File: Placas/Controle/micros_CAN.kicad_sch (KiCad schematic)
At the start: 8 parts, among them J10 Conn_01x02_Pin, J11 Conn_01x02_Pin, U10 ESP32-DevKitC, U8 ESP32-DevKitC, U9 TJA1050

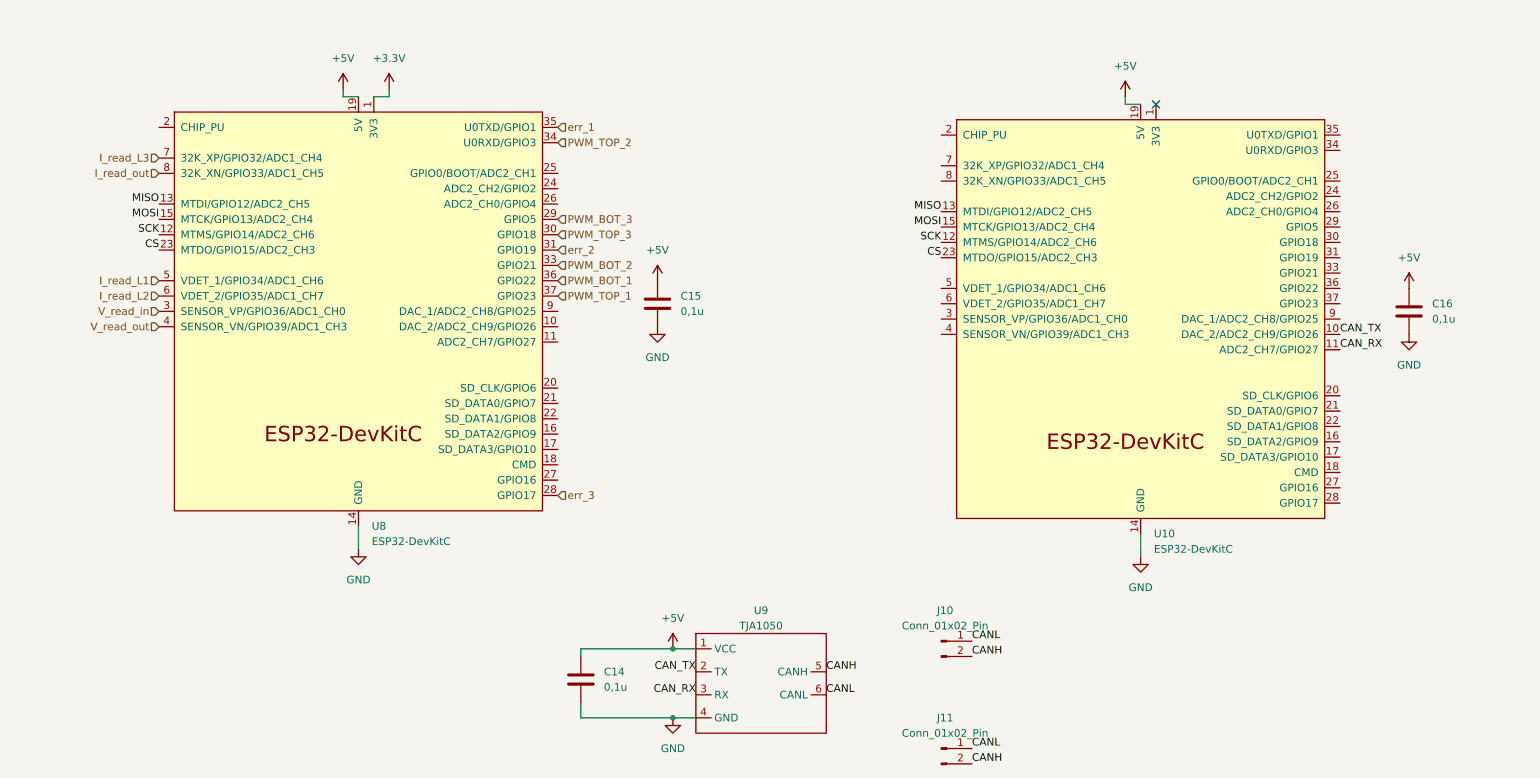
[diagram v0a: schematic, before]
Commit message: Adição de circuitos opcionais para PWM
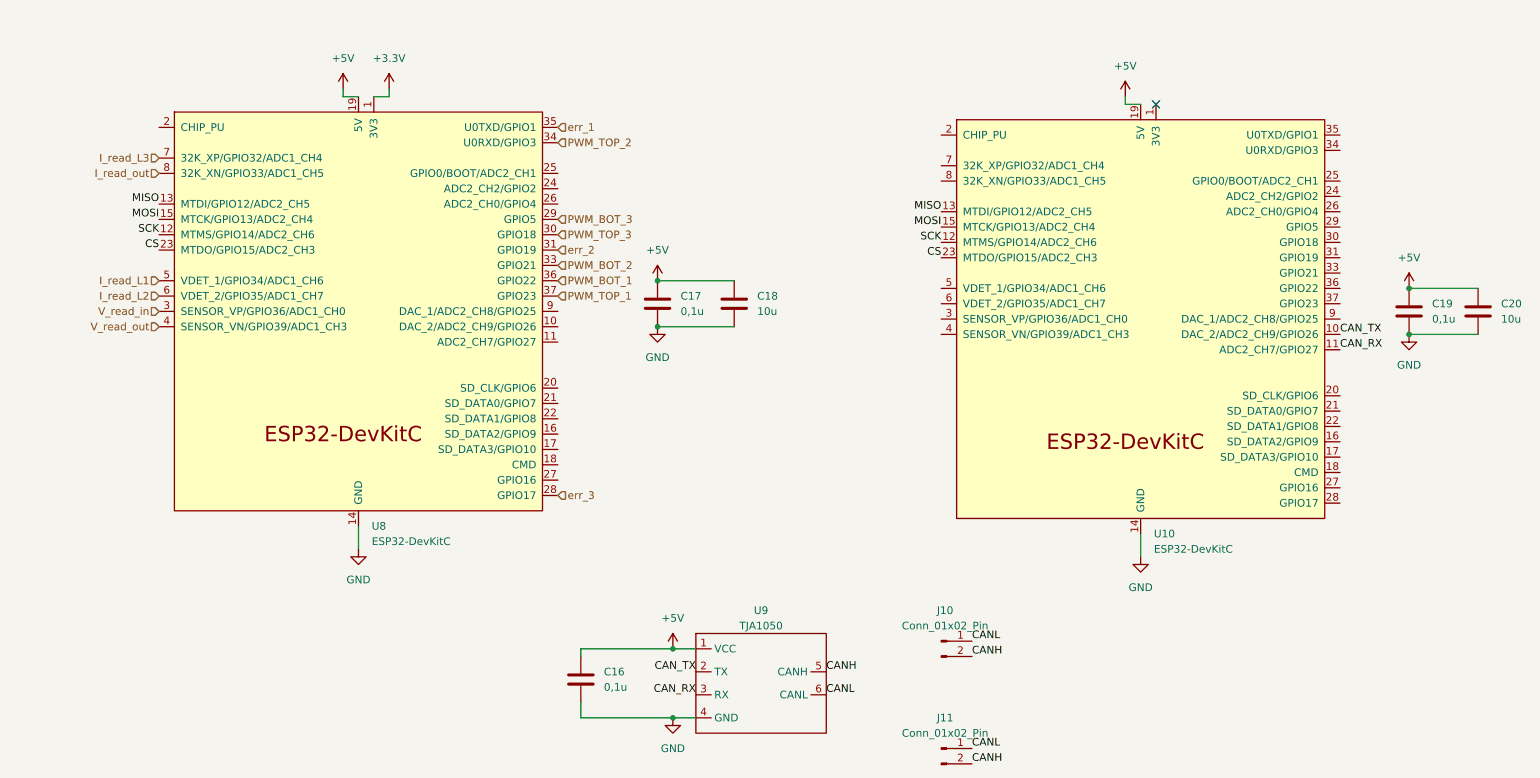
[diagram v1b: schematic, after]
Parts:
- added C18, C20: 10u, Capacitor_SMD:C_1210_3225Metric_Pad1.33x2.70mm_HandSolder, symbol Device:C
- C16: renamed from C14; footprint Capacitor_THT:C_Disc_D8.0mm_W5.0mm_P7.50mm -> Capacitor_SMD:C_0805_2012Metric_Pad1.18x1.45mm_HandSolder
- C17: renamed from C15; footprint Capacitor_THT:C_Disc_D8.0mm_W5.0mm_P7.50mm -> Capacitor_SMD:C_0805_2012Metric_Pad1.18x1.45mm_HandSolder
- C19: renamed from C16; footprint Capacitor_THT:C_Disc_D8.0mm_W5.0mm_P7.50mm -> Capacitor_SMD:C_0805_2012Metric_Pad1.18x1.45mm_HandSolder
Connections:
- net +5V: now also C18.1, C20.1
- net GND: now also C18.2, C20.2

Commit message: Modificações nas duas placas, adição de furos para montagem, melhora na posição dos micros e conectores para comunicação SPI
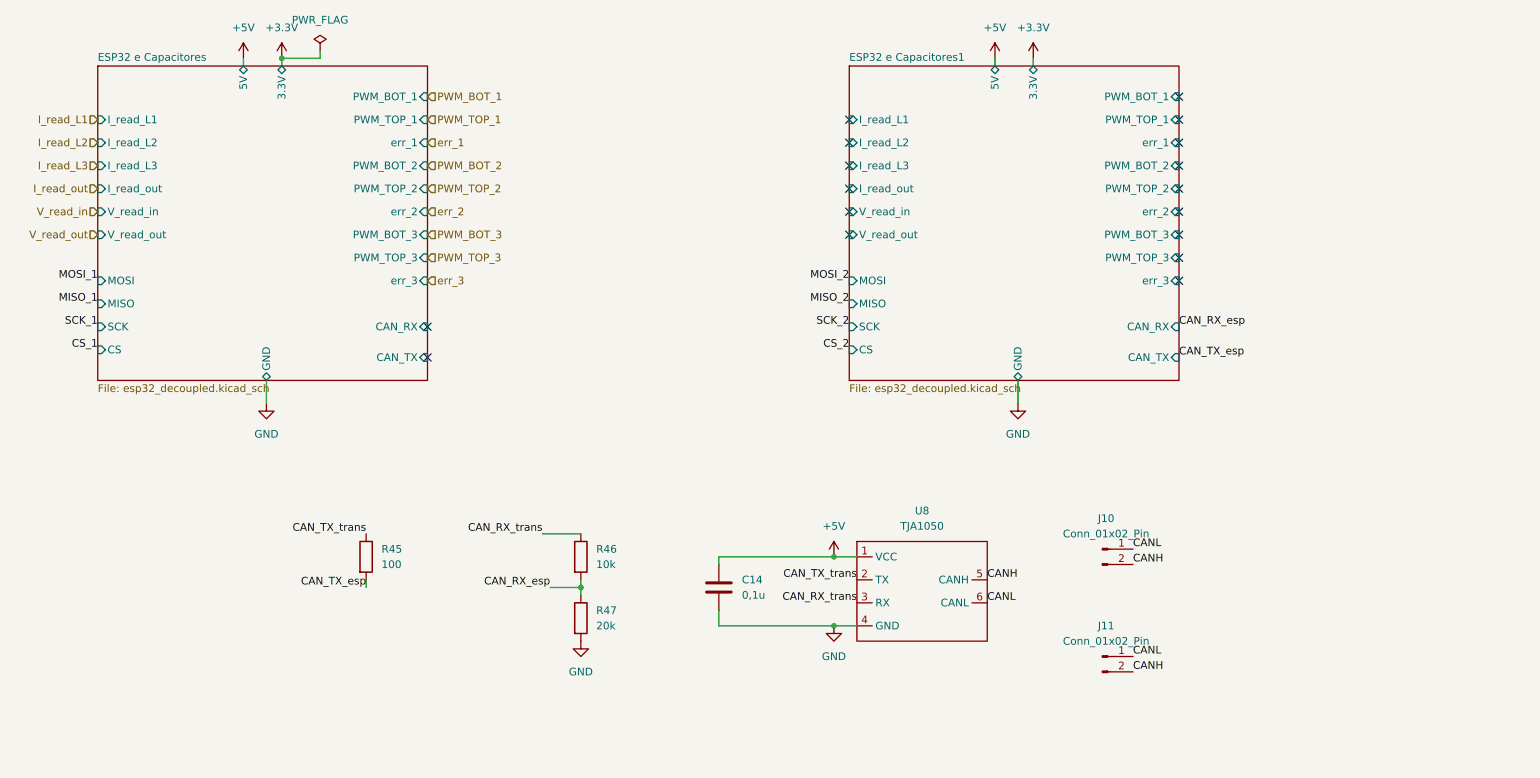
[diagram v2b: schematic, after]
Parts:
- removed C17, C19: 0,1u, Capacitor_SMD:C_0805_2012Metric_Pad1.18x1.45mm_HandSolder, symbol Device:C
- removed C18, C20: 10u, Capacitor_SMD:C_1210_3225Metric_Pad1.33x2.70mm_HandSolder, symbol Device:C
- removed U10, U8: ESP32-DevKitC, Espressif:ESP32-DevKitC, symbol PCM_Espressif:ESP32-DevKitC
- added R45: 100, Resistor_SMD:R_0805_2012Metric_Pad1.20x1.40mm_HandSolder, symbol Device:R
- added R46: 10k, Resistor_SMD:R_0805_2012Metric_Pad1.20x1.40mm_HandSolder, symbol Device:R
- added R47: 20k, Resistor_SMD:R_0805_2012Metric_Pad1.20x1.40mm_HandSolder, symbol Device:R
- U8: renamed from U9; symbol Modules:TJA1050_Module -> CAN Modules:TJA1050_Module
- renumbered C16 to C14
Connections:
- net GND: now also R47.2
- net CAN_RX renamed CAN_RX_trans
- net CAN_RX_trans: now also R46.1
- net CAN_TX renamed CAN_TX_trans
- net CAN_TX_trans: now also R45.1
- new net CAN_RX_esp: R46.2, R47.1
- new net CAN_TX_esp: R45.2
- no-connect marks 1 -> 17
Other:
- added sheet ESP32 e Capacitores (esp32_decoupled.kicad_sch)
- added sheet ESP32 e Capacitores1 (esp32_decoupled.kicad_sch)
- moved on the sheet: C14, J10, J11, U8

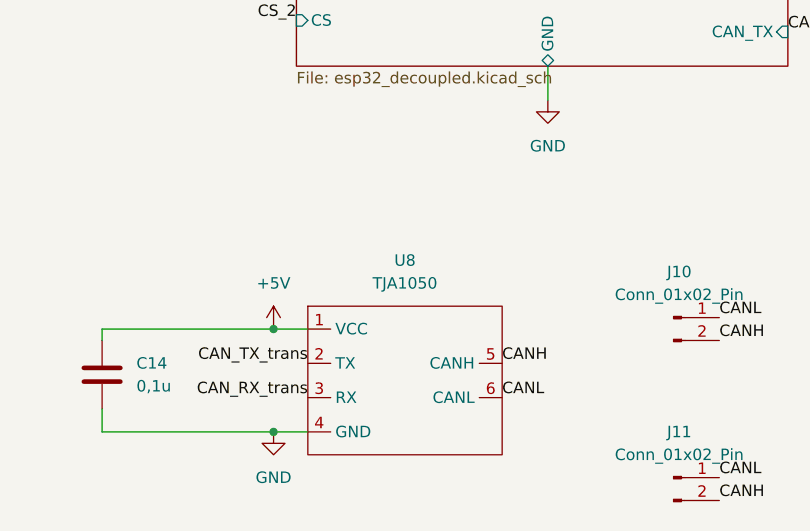
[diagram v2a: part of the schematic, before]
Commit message: Criação dos arquivos em C para o firmware dos dois micros e script em python para salvar aquisição dos dados e envio de comandos
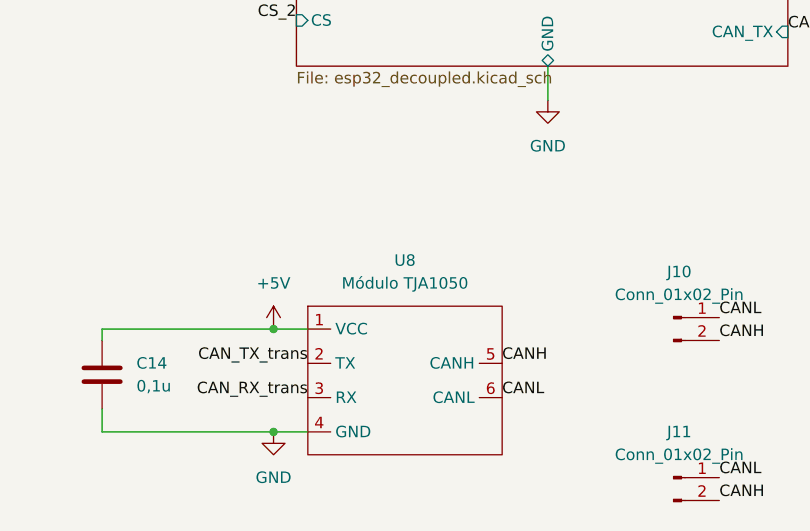
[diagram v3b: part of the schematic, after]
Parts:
- U8: value TJA1050 -> Módulo TJA1050
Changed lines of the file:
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@@
 			)
 		)
-		(property "Value" "TJA1050"
+		(property "Value" "Módulo TJA1050"
 			(at 172.085 120.65 0)
 			(effects

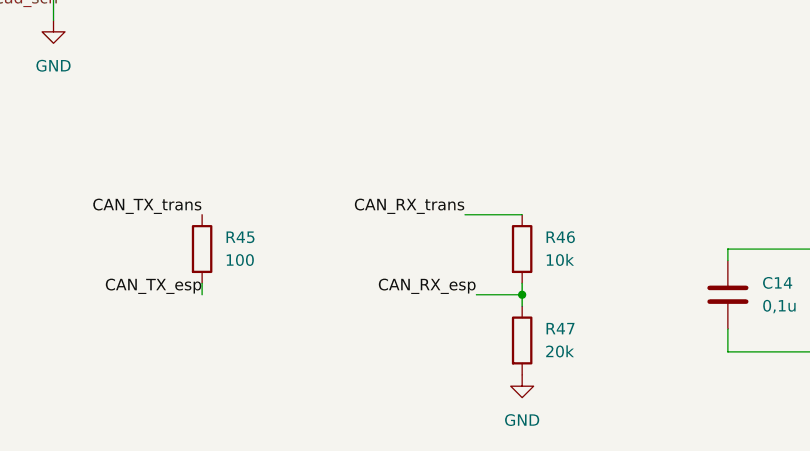
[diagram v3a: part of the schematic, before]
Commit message: Mudanças no firmware e calibração da tensão de entrada e saída
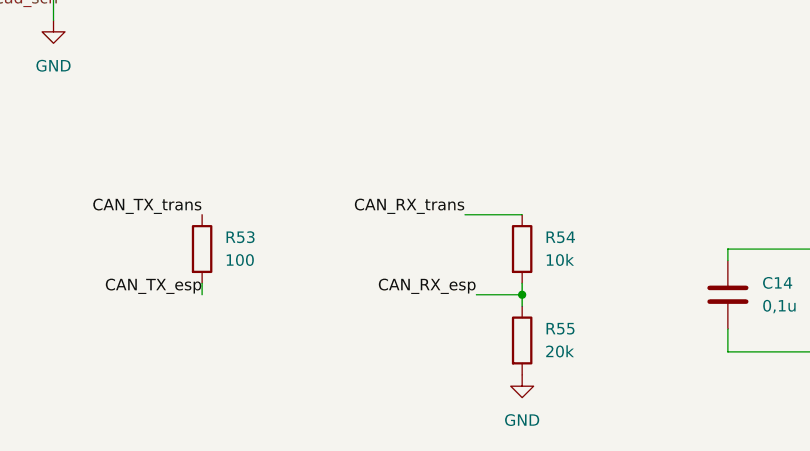
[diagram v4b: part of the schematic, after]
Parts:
- renumbered R45 to R53, R46 to R54, R47 to R55
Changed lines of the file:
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@@
 		(dnp no)
 		(fields_autoplaced yes)
-		(property "Reference" "#PWR73"
+		(property "Reference" "#PWR80"
 			(at 187.96 106.68 0)
 			(effects
@@
 			(project "Controle"
 				(path "/01568b53-f202-4f02-9c1a-9c10c7610b4b/4527811a-768c-47d7-9d21-cc6f720fbe2a"
-					(reference "#PWR73")
+					(reference "#PWR80")
 					(unit 1)
 				)
@@
 		(dnp no)
 		(fields_autoplaced yes)
-		(property "Reference" "R47"
+		(property "Reference" "R55"
 			(at 118.11 134.6199 0)
 			(effects
@@
 			(project ""
 				(path "/01568b53-f202-4f02-9c1a-9c10c7610b4b/4527811a-768c-47d7-9d21-cc6f720fbe2a"
-					(reference "R47")
+					(reference "R55")
 					(unit 1)
 				)
@@
 		(on_board yes)
 		(dnp no)
-		(property "Reference" "#PWR72"
+		(property "Reference" "#PWR79"
 			(at 184.15 46.99 0)
 			(effects
@@
 			(project "Controle"
 				(path "/01568b53-f202-4f02-9c1a-9c10c7610b4b/4527811a-768c-47d7-9d21-cc6f720fbe2a"
-					(reference "#PWR72")
+					(reference "#PWR79")
 					(unit 1)
 				)
@@
 		(dnp no)
 		(fields_autoplaced yes)
-		(property "Reference" "R46"
+		(property "Reference" "R54"
 			(at 118.11 124.4599 0)
 			(effects
@@
 			(project ""
 				(path "/01568b53-f202-4f02-9c1a-9c10c7610b4b/4527811a-768c-47d7-9d21-cc6f720fbe2a"
-					(reference "R46")
+					(reference "R54")
 					(unit 1)
 				)
@@
 		(on_board yes)
 		(dnp no)
-		(property "Reference" "#PWR74"
+		(property "Reference" "#PWR81"
 			(at 190.5 46.99 0)
 			(effects
@@
 			(project "Controle"
 				(path "/01568b53-f202-4f02-9c1a-9c10c7610b4b/4527811a-768c-47d7-9d21-cc6f720fbe2a"
-					(reference "#PWR74")
+					(reference "#PWR81")
 					(unit 1)
 				)
@@
 		(on_board yes)
 		(dnp no)
-		(property "Reference" "#PWR68"
+		(property "Reference" "#PWR75"
 			(at 66.04 46.99 0)
 			(effects
@@
 			(project ""
 				(path "/01568b53-f202-4f02-9c1a-9c10c7610b4b/4527811a-768c-47d7-9d21-cc6f720fbe2a"
-					(reference "#PWR68")
+					(reference "#PWR75")
 					(unit 1)
 				)
@@
 		(dnp no)
 		(fields_autoplaced yes)
-		(property "Reference" "#PWR69"
+		(property "Reference" "#PWR76"
 			(at 115.57 146.05 0)
 			(effects
@@
 			(project "Controle"
 				(path "/01568b53-f202-4f02-9c1a-9c10c7610b4b/4527811a-768c-47d7-9d21-cc6f720fbe2a"
-					(reference "#PWR69")
+					(reference "#PWR76")
 					(unit 1)
 				)
@@
 		(dnp no)
 		(fields_autoplaced yes)
-		(property "Reference" "#PWR67"
+		(property "Reference" "#PWR74"
 			(at 63.5 106.68 0)
 			(effects
@@
 			(project "Controle"
 				(path "/01568b53-f202-4f02-9c1a-9c10c7610b4b/4527811a-768c-47d7-9d21-cc6f720fbe2a"
-					(reference "#PWR67")
+					(reference "#PWR74")
 					(unit 1)
 				)
@@
 		(on_board yes)
 		(dnp no)
-		(property "Reference" "#PWR66"
+		(property "Reference" "#PWR73"
 			(at 59.69 46.99 0)
 			(effects
@@
 			(project "Controle"
 				(path "/01568b53-f202-4f02-9c1a-9c10c7610b4b/4527811a-768c-47d7-9d21-cc6f720fbe2a"
-					(reference "#PWR66")
+					(reference "#PWR73")
 					(unit 1)
 				)
@@
 		(dnp no)
 		(fields_autoplaced yes)
-		(property "Reference" "#PWR71"
+		(property "Reference" "#PWR78"
 			(at 157.48 143.51 0)
 			(effects
@@
 			(project "board"
 				(path "/01568b53-f202-4f02-9c1a-9c10c7610b4b/4527811a-768c-47d7-9d21-cc6f720fbe2a"
-					(reference "#PWR71")
+					(reference "#PWR78")
 					(unit 1)
 				)
@@
 		(dnp no)
 		(fields_autoplaced yes)
-		(property "Reference" "#PWR70"
+		(property "Reference" "#PWR77"
 			(at 157.48 129.54 0)
 			(effects
@@
 			(project "board"
 				(path "/01568b53-f202-4f02-9c1a-9c10c7610b4b/4527811a-768c-47d7-9d21-cc6f720fbe2a"
-					(reference "#PWR70")
+					(reference "#PWR77")
 					(unit 1)
 				)
@@
 		(dnp no)
 		(fields_autoplaced yes)
-		(property "Reference" "R45"
+		(property "Reference" "R53"
 			(at 82.55 124.4599 0)
 			(effects
@@
 			(project "Controle"
 				(path "/01568b53-f202-4f02-9c1a-9c10c7610b4b/4527811a-768c-47d7-9d21-cc6f720fbe2a"
-					(reference "R45")
-					(unit 1)
-				)
+					(reference "R53")
+					(unit 1)
+				)
